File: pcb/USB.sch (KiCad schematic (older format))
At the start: 99 parts, among them J0 12401598E4#2A, J2 1003-002-01100, J3 1003-002-01100, J4 12401598E4#2A, J5 12401598E4#2A, U0 USBLC6-2SC6, U10 AP22811AW5-7, U11 PTN5110DHQ, U12 PTN5110THQ, U13 PTN5110THQ, U14 SN74LVC1G08DCKR, U15 CBTL02043ABQ,115, U19 SN74LVC1G08DCKR, U2 USB7206, U20 AP22811AW5-7, U21 USBLC6-2SC6, U22 AP22811AW5-7, U23 AP22811AW5-7, U3 CBTL02043ABQ,115, U5 USBLC6-2SC6, U6 CBTL02043ABQ,115, U7 USBLC6-2SC6, U8 USBLC6-2SC6, U9 AP22811AW5-7, X1 ECS-3225MV-250-BN-TR

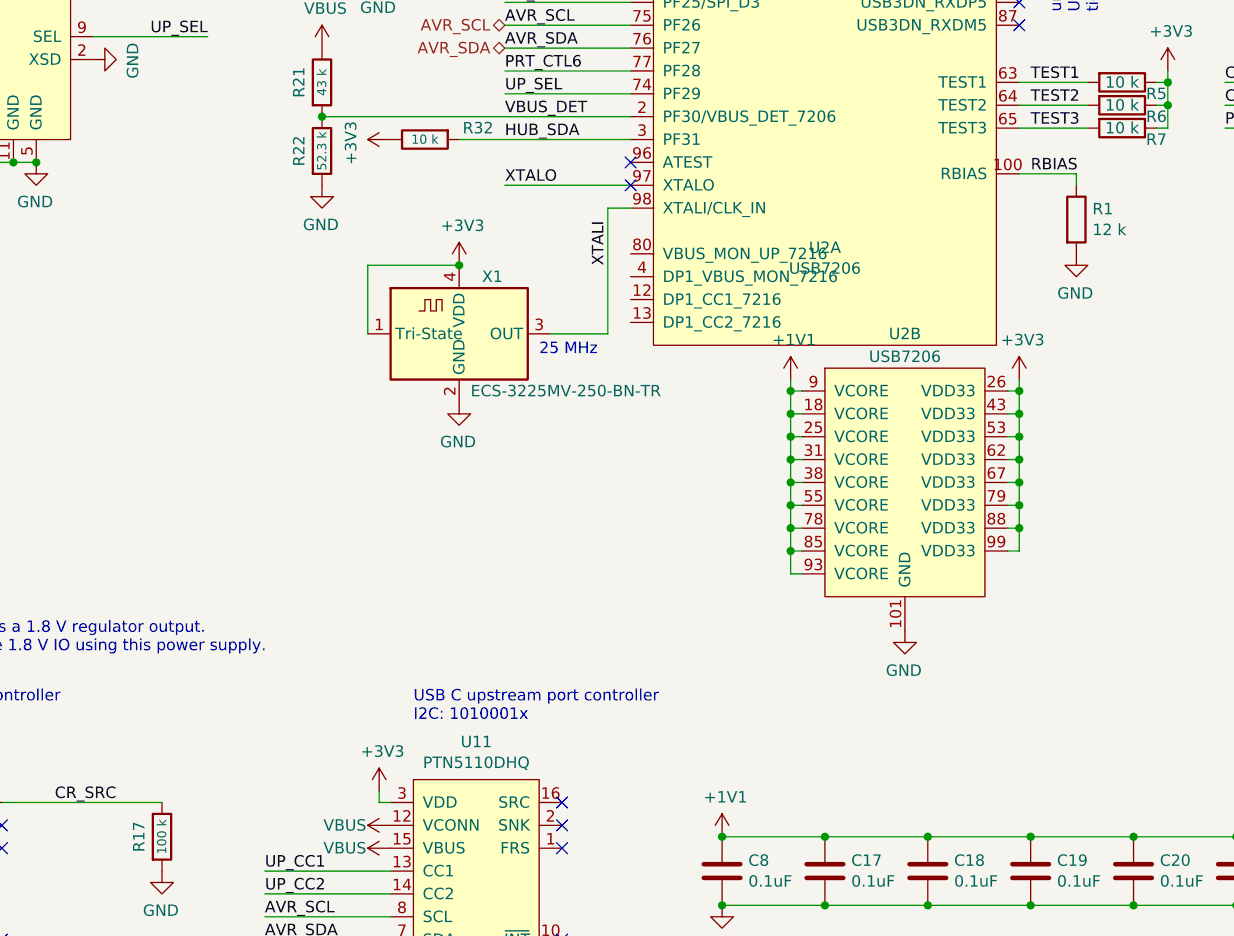
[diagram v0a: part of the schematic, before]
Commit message: add components to support USB7216 The USB7216 uses an alternate location, pin 80 for VBUS monitoring. This adds a voltage divider, R18 and R28 which should only be installed if a USB7216 is used. Pads for pull down resistors are provided for DP1_CC1/2, but will not be populated.
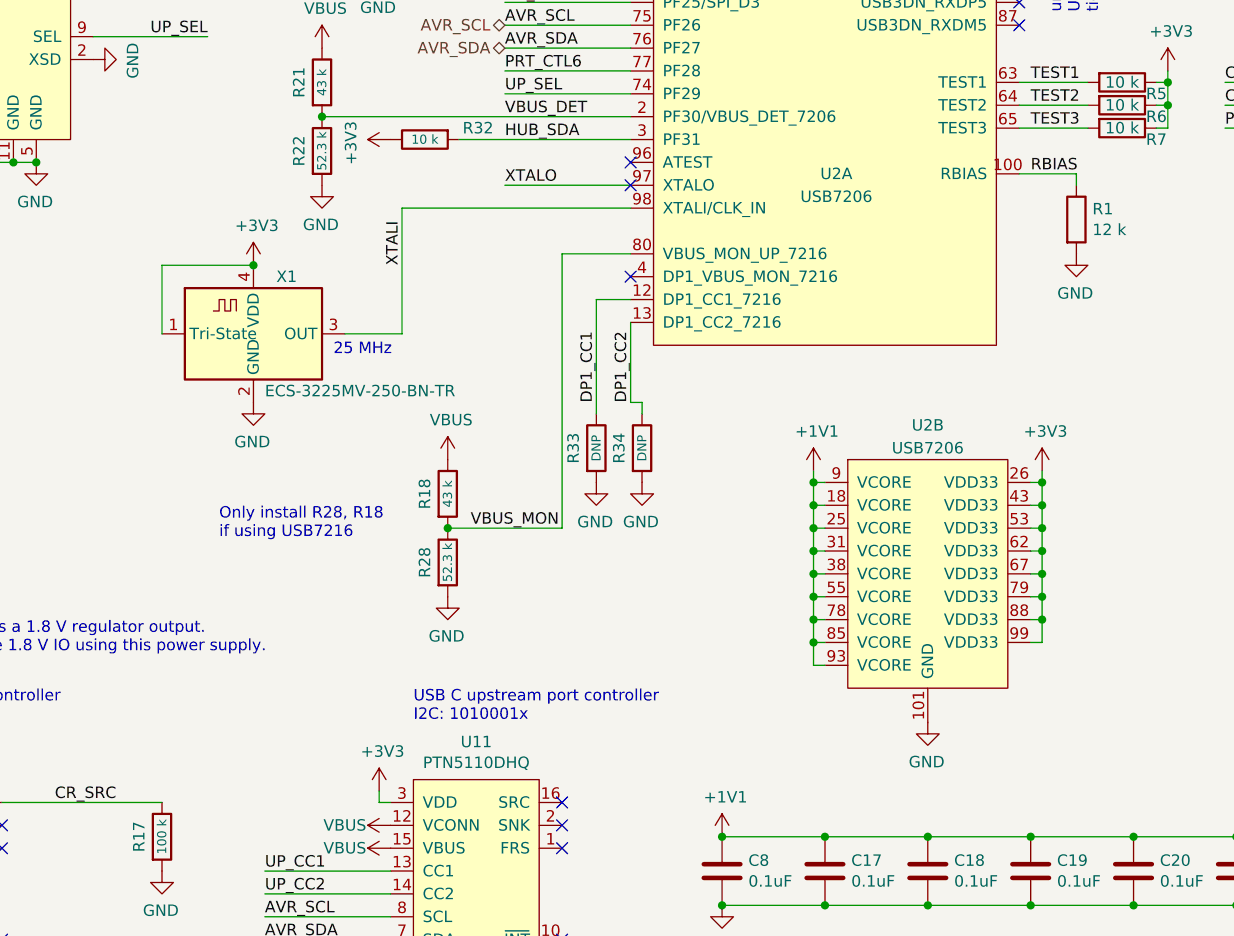
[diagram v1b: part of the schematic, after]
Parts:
- added R18: 43 k, launch:R_0402_1005Metric, symbol Device:R
- added R28: 52.3 k, launch:R_0402_1005Metric, symbol Device:R
- added R33, R34: DNP, launch:R_0402_1005Metric, symbol Device:R
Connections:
- net GND: now also R28.2, R33.2, R34.2
- net VBUS: now also R18.1
- net DP1_CC1: now reaches U2.12 (DP1_CC1_7216)
- net DP1_CC1: now also R33.1
- net DP1_CC2: now reaches U2.13 (DP1_CC2_7216)
- net DP1_CC2: now also R34.1
- net VBUS_MON: now reaches U2.80 (VBUS_MON_UP_7216)
- net VBUS_MON: now also R18.2, R28.1
- no-connect marks 41 -> 42
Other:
- note added: "Only install R28, R18\nif using USB7216"
- moved on the sheet: U2B, X1

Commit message: Ensure correct VBUS capacitor part number
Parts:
- C44, C45, C46, C47: value EEEFK0J151SR -> APXF6R3ARA151ME40G; Manufacturer Panasonic -> United Chemi-Con
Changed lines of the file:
@@
 P 13300 1100
 F 0 "C44" V 13450 1000 50  0000 L CNN
-F 1 "EEEFK0J151SR" H 13418 1055 50  0001 L CNN
+F 1 "APXF6R3ARA151ME40G" H 13418 1055 50  0001 L CNN
 F 2 "Capacitor_SMD:CP_Elec_5x3.9" H 13338 950 50  0001 C CNN
-F 3 "https://b2b-api.panasonic.eu/file_stream/pids/fileversion/3102" H 13300 1100 50  0001 C CNN
-F 4 "Panasonic" H 13300 1100 50  0001 C CNN "Manufacturer"
+F 3 "https://www.chemi-con.co.jp/en/products/detail-condenser.php?part_number=APXF6R3ARA151ME40G" H 13300 1100 50  0001 C CNN
+F 4 "United Chemi-Con" H 13300 1100 50  0001 C CNN "Manufacturer"
 	1    13300 1100
 	1    0    0    -1
@@
 P 12350 3050
 F 0 "C46" H 12468 3096 50  0000 L CNN
-F 1 "EEEFK0J151SR" H 12468 3005 50  0001 L CNN
+F 1 "APXF6R3ARA151ME40G" H 12468 3005 50  0001 L CNN
 F 2 "Capacitor_SMD:CP_Elec_5x3.9" H 12388 2900 50  0001 C CNN
-F 3 "https://b2b-api.panasonic.eu/file_stream/pids/fileversion/3102" H 12350 3050 50  0001 C CNN
-F 4 "Panasonic" H 12350 3050 50  0001 C CNN "Manufacturer"
+F 3 "https://www.chemi-con.co.jp/en/products/detail-condenser.php?part_number=APXF6R3ARA151ME40G" H 12350 3050 50  0001 C CNN
+F 4 "United Chemi-Con" H 12350 3050 50  0001 C CNN "Manufacturer"
 	1    12350 3050
 	1    0    0    -1
@@
 P 12350 6750
 F 0 "C47" H 12468 6796 50  0000 L CNN
-F 1 "EEEFK0J151SR" H 12468 6705 50  0001 L CNN
+F 1 "APXF6R3ARA151ME40G" H 12468 6705 50  0001 L CNN
 F 2 "Capacitor_SMD:CP_Elec_5x3.9" H 12388 6600 50  0001 C CNN
-F 3 "https://b2b-api.panasonic.eu/file_stream/pids/fileversion/3102" H 12350 6750 50  0001 C CNN
-F 4 "Panasonic" H 12350 6750 50  0001 C CNN "Manufacturer"
+F 3 "https://www.chemi-con.co.jp/en/products/detail-condenser.php?part_number=APXF6R3ARA151ME40G" H 12350 6750 50  0001 C CNN
+F 4 "United Chemi-Con" H 12350 6750 50  0001 C CNN "Manufacturer"
 	1    12350 6750
 	1    0    0    -1
@@
 P 7400 1250
 F 0 "C45" V 7550 1200 50  0000 L CNN
-F 1 "EEEFK0J151SR" H 7518 1205 50  0001 L CNN
+F 1 "APXF6R3ARA151ME40G" H 7518 1205 50  0001 L CNN
 F 2 "Capacitor_SMD:CP_Elec_5x3.9" H 7438 1100 50  0001 C CNN
-F 3 "https://b2b-api.panasonic.eu/file_stream/pids/fileversion/3102" H 7400 1250 50  0001 C CNN
-F 4 "Panasonic" H 7400 1250 50  0001 C CNN "Manufacturer"
+F 3 "https://www.chemi-con.co.jp/en/products/detail-condenser.php?part_number=APXF6R3ARA151ME40G" H 7400 1250 50  0001 C CNN
+F 4 "United Chemi-Con" H 7400 1250 50  0001 C CNN "Manufacturer"
 	1    7400 1250
 	1    0    0    -1

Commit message: Fix library references for symbols renamed in upstream also remove cache from gitignore, include in repo in case user's libaries don't align.
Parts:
- C44, C45, C46, C47: symbol Device:CP -> Device:C_Polarized
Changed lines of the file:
@@
 	13150 1200 13100 1200
 Wire Wire Line
-	13150 950  13300 950
-Wire Wire Line
 	13550 1150 13550 800
 Wire Wire Line
@@
 	1    0    0    -1
 $EndComp
-Wire Wire Line
-	13150 2900 12350 2900
 Connection ~ 13150 2900
 $Comp
@@
 NoConn ~ 7400 4500
 $Comp
-L Device:CP C44
+L Device:C_Polarized C44
 U 1 1 5F253341
 P 13300 1100
@@
 	1    0    0    -1
 $EndComp
-Connection ~ 13300 950
 $Comp
 L power:GND #PWR?
@@
 NoConn ~ 7100 9700
 $Comp
-L Device:CP C46
+L Device:C_Polarized C46
 U 1 1 5F485345
 P 12350 3050
@@
 	-1   0    0    -1
 $EndComp
-Connection ~ 12350 2900
-Wire Wire Line
-	12350 2900 12150 2900
 $Comp
 L power:GND #PWR?
@@
 Wire Wire Line
 	13150 7250 13150 6600
-Wire Wire Line
-	13150 6600 12350 6600
 Connection ~ 13150 6600
 Wire Wire Line
@@
 	10450 6850 10500 6850
 $Comp
-L Device:CP C47
+L Device:C_Polarized C47
 U 1 1 5F88AF4F
 P 12350 6750
@@
 	-1   0    0    -1
 $EndComp
-Connection ~ 12350 6600
-Wire Wire Line
-	12350 6600 12150 6600
 Text Label 12600 6850 0    50   ~ 0
 CL_D-
@@
 Wire Wire Line
 	2450 4050 1700 4050
-Wire Wire Line
-	7400 1100 7800 1100
-Connection ~ 7400 1100
 $Comp
 L power:GND #PWR?
@@
 AL_VBUS
 Wire Wire Line
-	7250 1100 7400 1100
-Wire Wire Line
 	6700 1750 6250 1750
 Wire Wire Line
@@
 $EndComp
 Wire Wire Line
-	13300 950  13700 950
-Wire Wire Line
 	11850 850  11900 850
 Wire Wire Line
@@
 150 uF
 $Comp
-L Device:CP C45
+L Device:C_Polarized C45
 U 1 1 5F427BA1
 P 7400 1250
@@
 Wire Wire Line
 	7400 7600 7400 7950
+Wire Wire Line
+	13150 950  13300 950
+Wire Wire Line
+	12150 2900 12350 2900
+Wire Wire Line
+	12150 6600 12350 6600
+Wire Wire Line
+	7250 1100 7400 1100
+Connection ~ 13300 950
+Wire Wire Line
+	13300 950  13700 950
+Connection ~ 12350 6600
+Wire Wire Line
+	12350 6600 13150 6600
+Connection ~ 7400 1100
+Wire Wire Line
+	7400 1100 7800 1100
+Connection ~ 12350 2900
+Wire Wire Line
+	12350 2900 13150 2900
+Connection ~ 18200 5350
+Connection ~ 17400 -4650
 $EndSCHEMATC

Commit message: use AP3441LSHE-7B DC-DC switching to available part from long lead time part adds 2 22 uF 0805 capacitors as well
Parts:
- U2: value USB7206 -> USB7216C
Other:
- note added: "If using USB7206,\ndo not install R28, R18"
- note removed: "Only install R28, R18\nif using USB7216"
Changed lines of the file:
@@
 encoding utf-8
 Sheet 2 3
-Title ""
-Date "2021-05-27"
-Rev ""
-Comp ""
+Title "Launch"
+Date "2021-09-13"
+Rev "1.4"
+Comp "System76"
 Comment1 ""
 Comment2 ""
@@
 	2250 4350 1700 4350
 $Comp
-L launch:USB7206 U2
-U 2 1 5F63C1C2
-P 8700 8700
-F 0 "U2" H 8700 9350 50  0000 C CNN
-F 1 "USB7206" H 8700 9250 50  0000 C CNN
-F 2 "launch:QFN-100-1EP_12x12mm_P0.4mm_EP8x8mm" H 7950 10900 50  0001 C CNN
-F 3 "${KIPRJMOD}/docs/USB7206.pdf" H 7950 10900 50  0001 C CNN
-F 4 "Microchip" H 8700 8700 50  0001 C CNN "Manufacturer"
-	2    8700 8700
-	1    0    0    -1
-$EndComp
-$Comp
 L power:GND #PWR?
 U 1 1 5F63EDF7
@@
 Text Notes 6100 7750 0    50   ~ 0
 25 MHz
-$Comp
-L launch:USB7206 U2
-U 1 1 5F63AD77
-P 8250 4800
-F 0 "U2" H 8300 2650 50  0000 C CNN
-F 1 "USB7206" H 8300 2550 50  0000 C CNN
-F 2 "launch:QFN-100-1EP_12x12mm_P0.4mm_EP8x8mm" H 7500 7000 50  0001 C CNN
-F 3 "${KIPRJMOD}/docs/USB7206.pdf" H 7500 7000 50  0001 C CNN
-F 4 "Microchip" H 8250 4800 50  0001 C CNN "Manufacturer"
-	1    8250 4800
-	1    0    0    -1
-$EndComp
 Text Notes 6250 6050 1    50   ~ 0
 unused\nSPI tie off
@@
 NoConn ~ 7400 7400
 Text Notes 5600 8550 0    50   ~ 0
-Only install R28, R18\nif using USB7216
+If using USB7206,\ndo not install R28, R18
 Connection ~ 6600 8500
 $Comp
@@
 Wire Wire Line
 	12350 2900 13150 2900
-Connection ~ 18200 5350
-Connection ~ 17400 -4650
+$Comp
+L launch:USB7206 U2
+U 2 1 5F63C1C2
+P 8700 8700
+F 0 "U2" H 8700 9350 50  0000 C CNN
+F 1 "USB7216C" H 8700 9250 50  0000 C CNN
+F 2 "launch:QFN-100-1EP_12x12mm_P0.4mm_EP8x8mm" H 7950 10900 50  0001 C CNN
+F 3 "${KIPRJMOD}/docs/USB7206.pdf" H 7950 10900 50  0001 C CNN
+F 4 "Microchip" H 8700 8700 50  0001 C CNN "Manufacturer"
+	2    8700 8700
+	1    0    0    -1
+$EndComp
+$Comp
+L launch:USB7206 U2
+U 1 1 5F63AD77
+P 8250 4800
+F 0 "U2" H 8300 2650 50  0000 C CNN
+F 1 "USB7216C" H 8300 2550 50  0000 C CNN
+F 2 "launch:QFN-100-1EP_12x12mm_P0.4mm_EP8x8mm" H 7500 7000 50  0001 C CNN
+F 3 "${KIPRJMOD}/docs/USB7206.pdf" H 7500 7000 50  0001 C CNN
+F 4 "Microchip" H 8250 4800 50  0001 C CNN "Manufacturer"
+	1    8250 4800
+	1    0    0    -1
+$EndComp
 $EndSCHEMATC
